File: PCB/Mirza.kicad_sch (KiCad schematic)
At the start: 105 parts, among them J1 In, J2 Out, J3 Power, Q1 BCM857BS, Q13 2SC3324, Q14 2SA1312, Q15 2SA1312, Q16 2SA1312, Q17 2SC3324, Q18 2SC3324, Q2 BCM847BS, Q21 2SA1312, Q22 2SC3324, Q23 2SC3324, Q24 2SA1312, Q25 D45H11, Q26 D44H11, Q3 2SA1312, Q4 2SC3324, Q5 2SC3324, Q6 2SC3324, Q7 2SA1312, Q8 2SA1312, U1 ADA4522-1

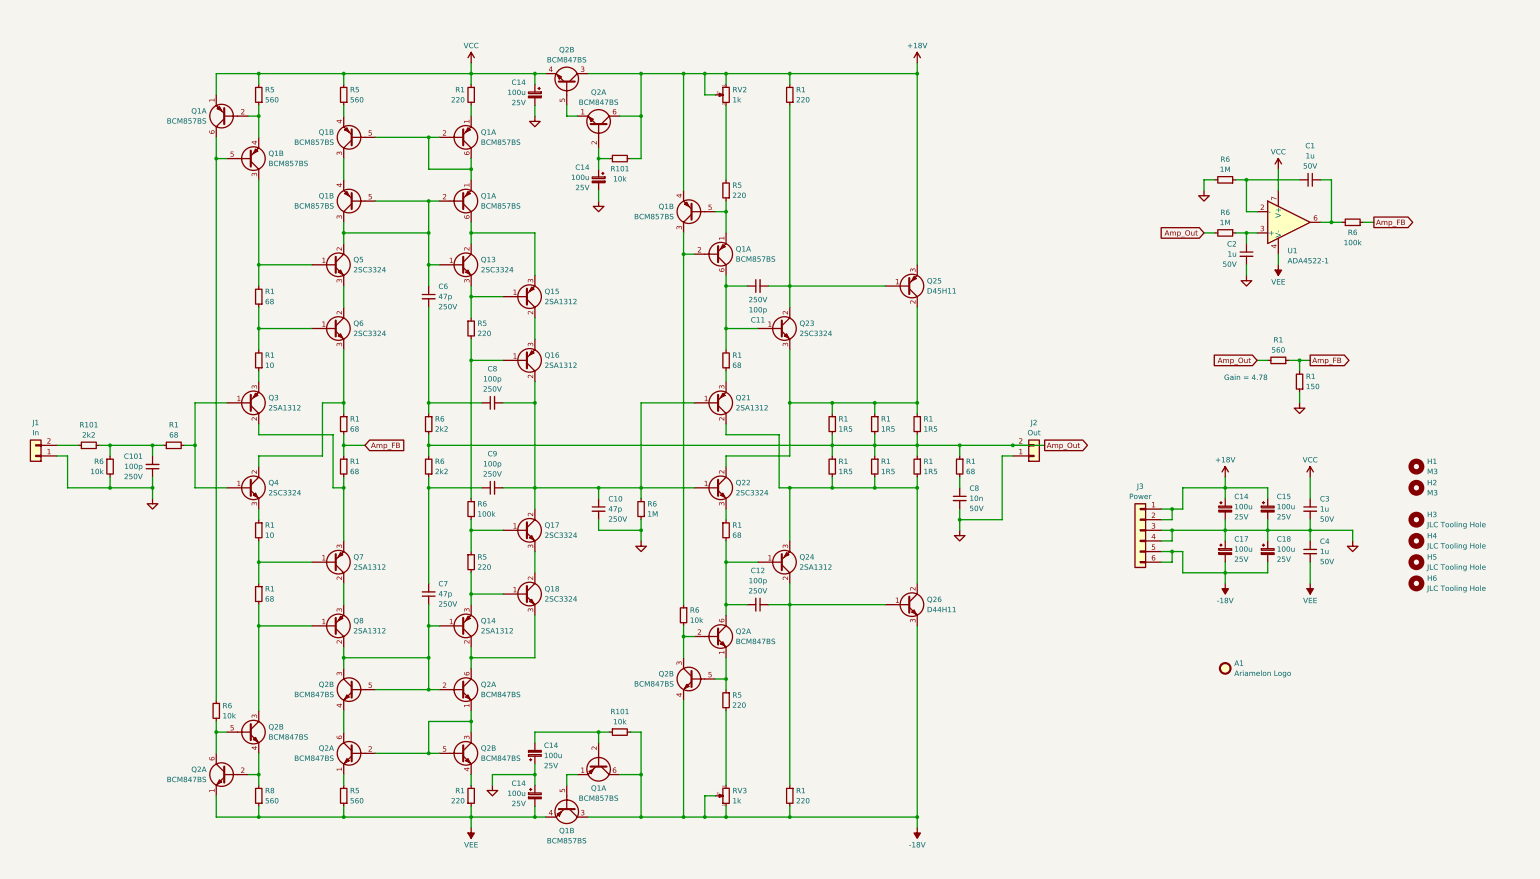
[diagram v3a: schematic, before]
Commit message: 20/09/2023 update
Shortened board by removing one pair of capacitors and increasing the size of the other and reducing the number of emitter resistors.
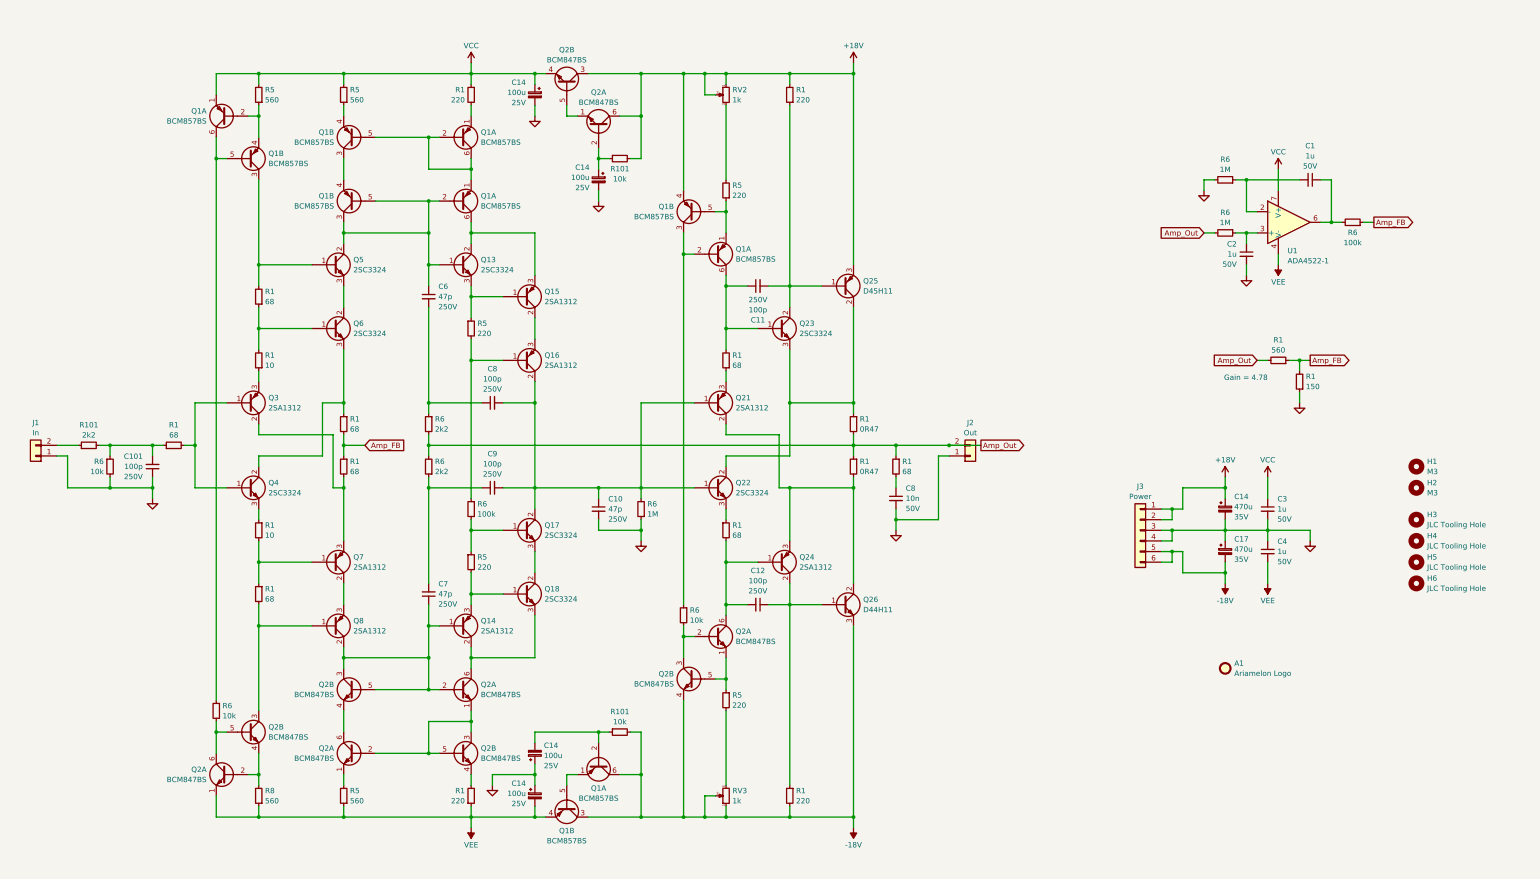
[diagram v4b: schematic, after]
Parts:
- removed C15, C18: 100u, Ariamelon-Device:CP_Radial_D6.3mm_P2.50mm, symbol Device:C_Polarized_Small
- removed R1 (x4): 1R5, Resistor_SMD:R_MiniMELF_MMA-0204, symbol Device:R_Small
- C14, C17: value 100u -> 470u; footprint Ariamelon-Device:CP_Radial_D6.3mm_P2.50mm -> Ariamelon-Device:CP_Radial_D8.0mm_P3.50mm_P5.00mm; LCSC C264049 -> C178717; Manufacturer No. EEUFR1E101 -> EEUFR1V471LB; Voltage 25V -> 35V
- R1: value 1R5 -> 0R47; LCSC C3008833 -> C2089943; Manufacturer No. MMA02040C1508FB300 -> MMA02040C4707FB300
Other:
- moved on the sheet: C3, C4, C8, J2, Q25, Q26, R1

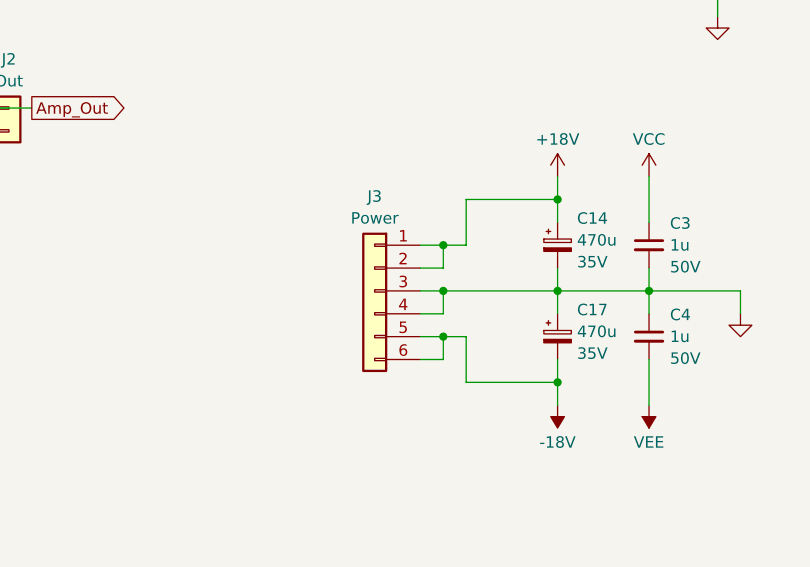
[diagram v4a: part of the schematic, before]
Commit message: 22/03/2023 update
Changed power connector to phoenix terminal block.
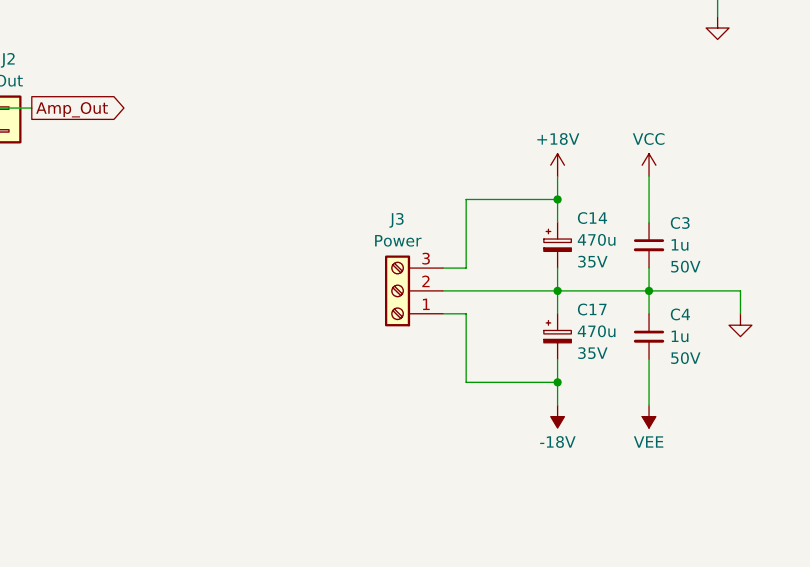
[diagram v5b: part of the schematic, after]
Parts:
- removed J3: Power, Ariamelon-Connector:JST_XH_B6B-XH-A_1x06_P2.50mm_Vertical_MiddleGND, symbol Connector_Generic:Conn_01x06
- added J3: Power, Ariamelon-Connector:TerminalBlock_Phoenix_MPT-0,5-3-2.54_1x03_P2.54mm_Horizontal_MiddleGND, symbol Connector:Screw_Terminal_01x03
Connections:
- net +18V: now also J3.3 (Pin_3)
- net -18V: now also J3.1 (Pin_1)
- net GND: now also J3.2 (Pin_2)
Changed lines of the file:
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@@
   (title_block
     (title "Mirza Current-Feedback Amplifier Module")
-    (date "2023-09-20")
+    (date "2023-09-22")
     (rev "V1.0")
     (company "Created by Ariamelon (https://github.com/Ariamelon/Mirza/)")
@@
   (junction (at 109.22 60.96) (diameter 0) (color 0 0 0 0)
   )
-  (junction (at 307.34 165.1) (diameter 0) (color 0 0 0 0)
-  )
   (junction (at 231.14 60.96) (diameter 0) (color 0 0 0 0)
   )
@@
   (junction (at 320.04 170.18) (diameter 0) (color 0 0 0 0)
   )
-  (junction (at 307.34 170.18) (diameter 0) (color 0 0 0 0)
-  )
   (junction (at 63.5 149.86) (diameter 0) (color 0 0 0 0)
   )
@@
   (junction (at 129.54 91.44) (diameter 0) (color 0 0 0 0)
   )
-  (junction (at 307.34 175.26) (diameter 0) (color 0 0 0 0)
-  )
   (junction (at 200.66 111.76) (diameter 0) (color 0 0 0 0)
   )
@@
     (stroke (width 0) (type default))
   )
-  (wire (pts (xy 307.34 175.26) (xy 309.88 175.26))
+  (wire (pts (xy 307.34 172.72) (xy 309.88 172.72))
     (stroke (width 0) (type default))
   )
@@
     (stroke (width 0) (type default))
   )
-  (wire (pts (xy 307.34 165.1) (xy 304.8 165.1))
-    (stroke (width 0) (type default))
-  )
-  (wire (pts (xy 307.34 172.72) (xy 307.34 170.18))
-    (stroke (width 0) (type default))
-  )
   (wire (pts (xy 144.78 228.6) (xy 154.94 228.6))
     (stroke (width 0) (type default))
@@
     (stroke (width 0) (type default))
   )
-  (wire (pts (xy 307.34 165.1) (xy 307.34 167.64))
-    (stroke (width 0) (type default))
-  )
   (wire (pts (xy 320.04 170.18) (xy 330.2 170.18))
     (stroke (width 0) (type default))
@@
     (stroke (width 0) (type default))
   )
-  (wire (pts (xy 304.8 172.72) (xy 307.34 172.72))
-    (stroke (width 0) (type default))
-  )
   (wire (pts (xy 88.9 60.96) (xy 109.22 60.96))
     (stroke (width 0) (type default))
@@
     (stroke (width 0) (type default))
   )
-  (wire (pts (xy 307.34 165.1) (xy 309.88 165.1))
+  (wire (pts (xy 307.34 167.64) (xy 309.88 167.64))
     (stroke (width 0) (type default))
   )
@@
     (stroke (width 0) (type default))
   )
-  (wire (pts (xy 309.88 180.34) (xy 309.88 175.26))
+  (wire (pts (xy 309.88 180.34) (xy 309.88 172.72))
     (stroke (width 0) (type default))
   )
@@
     (stroke (width 0) (type default))
   )
-  (wire (pts (xy 307.34 177.8) (xy 304.8 177.8))
-    (stroke (width 0) (type default))
-  )
   (wire (pts (xy 180.34 162.56) (xy 180.34 160.02))
     (stroke (width 0) (type default))
@@
     (stroke (width 0) (type default))
   )
-  (wire (pts (xy 309.88 165.1) (xy 309.88 160.02))
+  (wire (pts (xy 309.88 167.64) (xy 309.88 160.02))
     (stroke (width 0) (type default))
   )
@@
     (stroke (width 0) (type default))
   )
-  (wire (pts (xy 307.34 175.26) (xy 307.34 177.8))
-    (stroke (width 0) (type default))
-  )
   (wire (pts (xy 200.66 111.76) (xy 205.74 111.76))
     (stroke (width 0) (type default))
@@
     (stroke (width 0) (type default))
   )
-  (wire (pts (xy 304.8 175.26) (xy 307.34 175.26))
-    (stroke (width 0) (type default))
-  )
   (wire (pts (xy 63.5 160.02) (xy 63.5 157.48))
     (stroke (width 0) (type default))
@@
     (stroke (width 0) (type default))
   )
-  (wire (pts (xy 304.8 170.18) (xy 307.34 170.18))
-    (stroke (width 0) (type default))
-  )
   (wire (pts (xy 88.9 154.94) (xy 88.9 152.4))
     (stroke (width 0) (type default))
@@
     (stroke (width 0) (type default))
   )
-  (wire (pts (xy 307.34 167.64) (xy 304.8 167.64))
-    (stroke (width 0) (type default))
-  )
   (wire (pts (xy 139.7 68.58) (xy 139.7 71.12))
     (stroke (width 0) (type default))
@@
     )
   )
+  (symbol (lib_id "Connector:Screw_Terminal_01x03") (at 302.26 170.18 180) (unit 1)
+    (in_bom yes) (on_board yes) (dnp no) (fields_autoplaced)
+    (property "Reference" "J3" (at 302.26 162.2257 0)
+      (effects (font (size 1.27 1.27)))
+    )
+    (property "Value" "Power" (at 302.26 164.6499 0)
+      (effects (font (size 1.27 1.27)))
+    )
+    (property "Footprint" "Ariamelon-Connector:TerminalBlock_Phoenix_MPT-0,5-3-2.54_1x03_P2.54mm_Horizontal_MiddleGND" (at 302.26 170.18 0)
+      (effects (font (size 1.27 1.27)) hide)
+    )
+    (property "Datasheet" "~" (at 302.26 170.18 0)
+      (effects (font (size 1.27 1.27)) hide)
+    )
+    (pin "1")
+    (pin "2")
+    (pin "3")
+    (instances
+      (project "Mirza"
+        (path "/fe9fc43f-1188-4d03-8e81-9a6232eb6dc0"
+          (reference "J3") (unit 1)
+        )
+      )
+    )
+  )
   (symbol (lib_id "Device:R_Small") (at 88.9 185.42 0) (mirror y) (unit 1)
     (in_bom yes) (on_board yes) (dnp no)
@@
         )
       )
-    )
-  )
-  (symbol (lib_id "Connector_Generic:Conn_01x06") (at 299.72 170.18 0) (mirror y) (unit 1)
-    (in_bom yes) (on_board yes) (dnp no) (fields_autoplaced)
-    (property "Reference" "J3" (at 299.72 159.6857 0)
-      (effects (font (size 1.27 1.27)))
-    )
-    (property "Value" "Power" (at 299.72 162.1099 0)
-      (effects (font (size 1.27 1.27)))
-    )
-    (property "Footprint" "Ariamelon-Connector:JST_XH_B6B-XH-A_1x06_P2.50mm_Vertical_MiddleGND" (at 299.72 170.18 0)
-      (effects (font (size 1.27 1.27)) hide)
-    )
-    (property "Datasheet" "~" (at 299.72 170.18 0)
-      (effects (font (size 1.27 1.27)) hide)
-    )
-    (pin "1")
-    (pin "2")
-    (pin "3")
-    (pin "4")
-    (pin "5")
-    (pin "6")
-    (instances
-      (project "Mirza"
-        (path "/fe9fc43f-1188-4d03-8e81-9a6232eb6dc0"
-          (reference "J3") (unit 1)
-        )
-      )

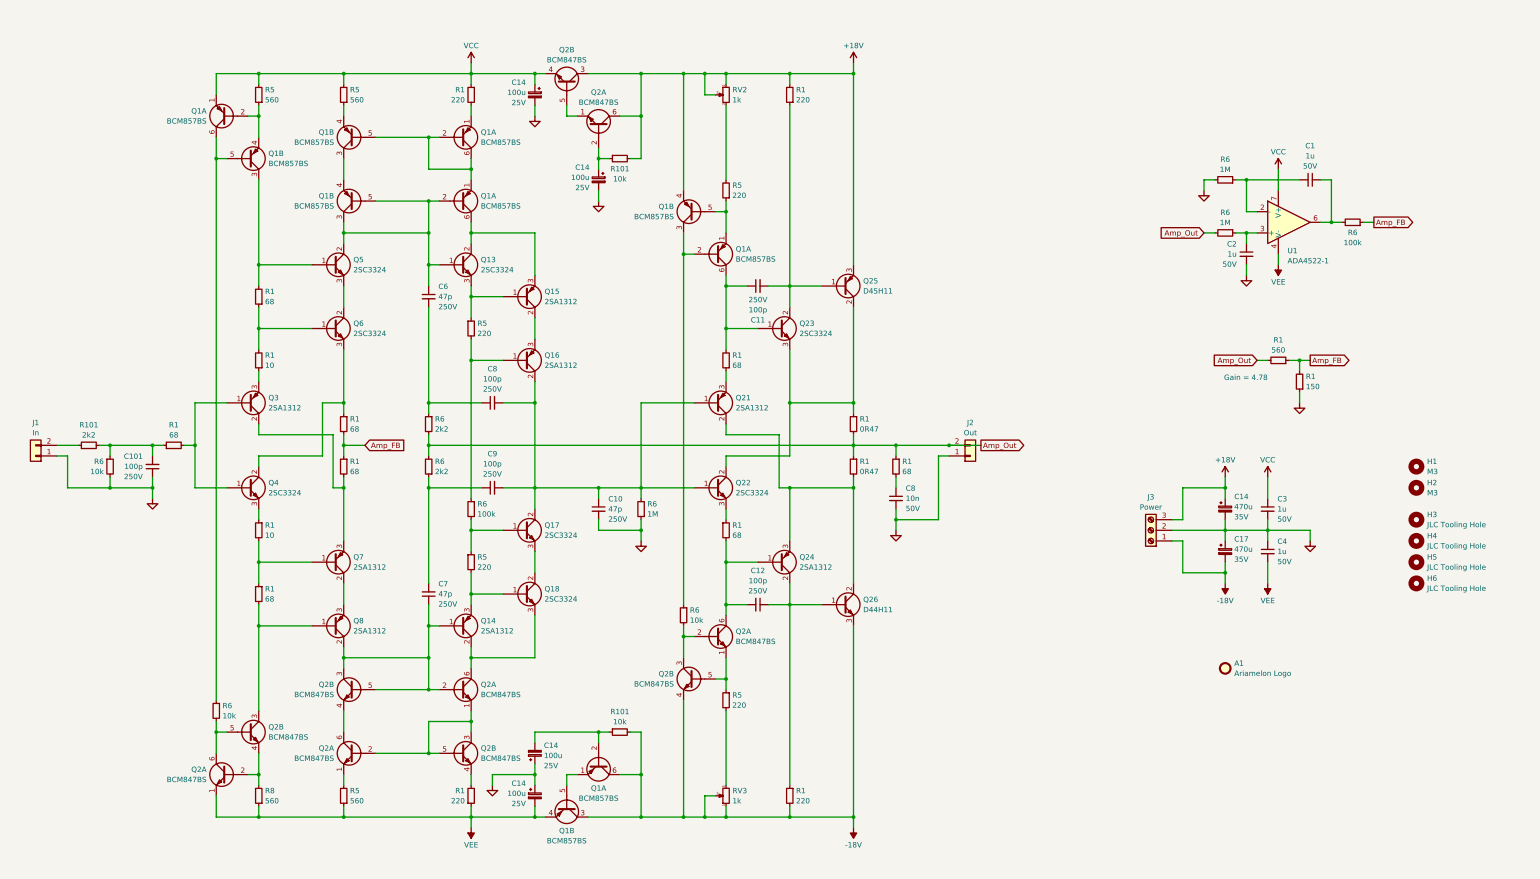
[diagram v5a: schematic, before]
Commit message: 23/09/2023 update
Changed all dual transistors to BCM847DS/BCM857DS for easier soldering.
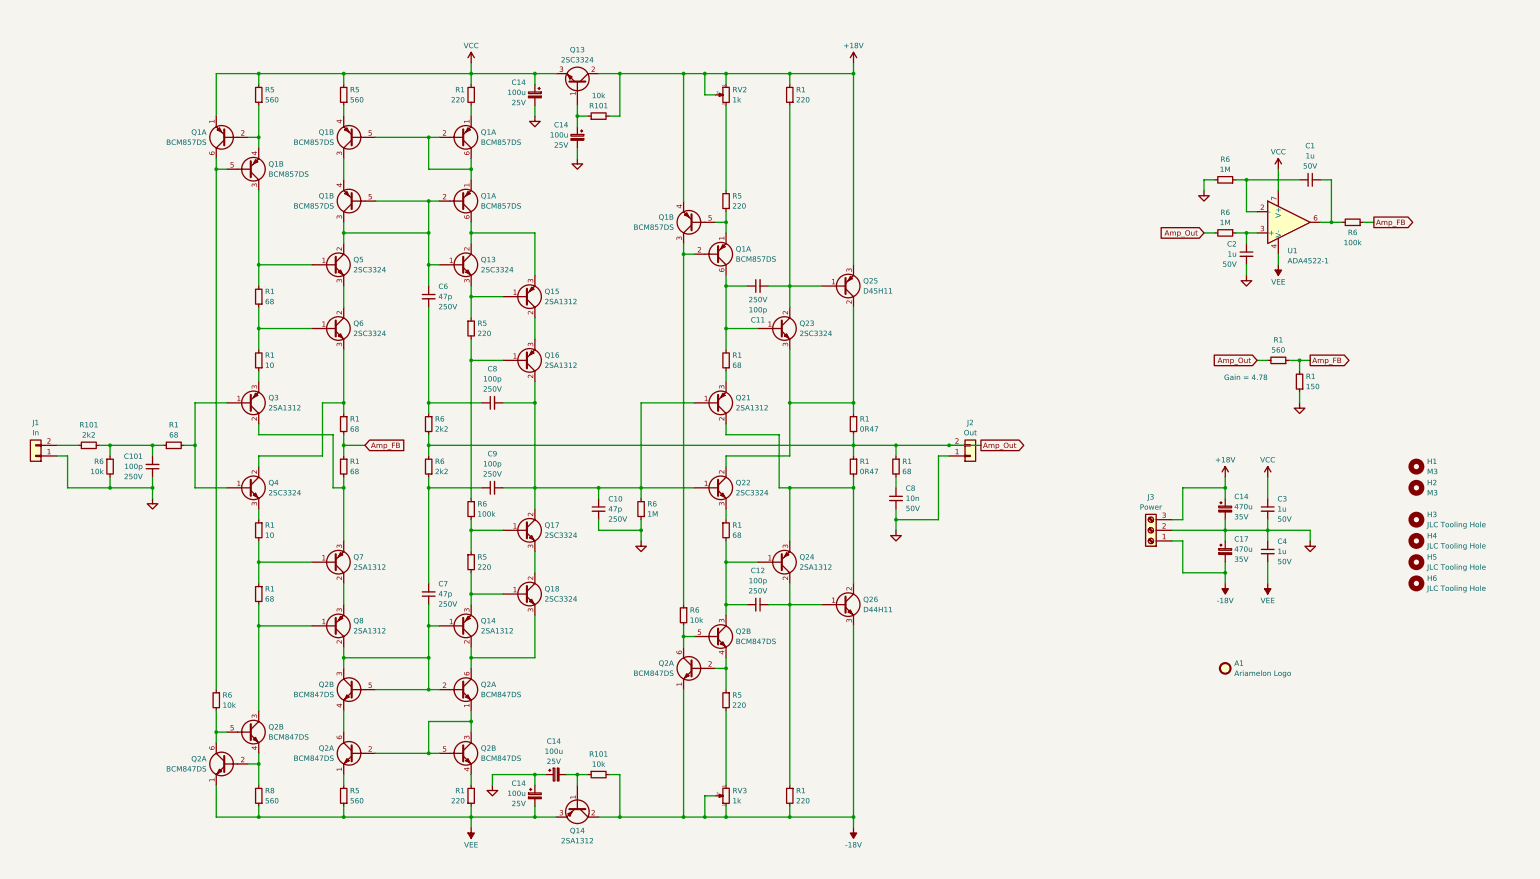
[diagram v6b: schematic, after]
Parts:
- removed Q1 (x5): BCM857BS, Ariamelon-Package:SOT-363_SC-70-6, symbol Transistor_BJT:BC857BS
- removed Q2 (x5): BCM847BS, Ariamelon-Package:SOT-363_SC-70-6, symbol Transistor_BJT:BC847BS
- added Q1 (x4): BCM857DS, Ariamelon-Package:SOT-23-6, symbol Device:Q_Dual_PNP_PNP_E1B1C2E2B2C1
- added Q13: 2SC3324, Ariamelon-Package:SOT-23-3, symbol Device:Q_NPN_BCE
- added Q14: 2SA1312, Ariamelon-Package:SOT-23-3, symbol Device:Q_PNP_BCE
- added Q2 (x4): BCM847DS, Ariamelon-Package:SOT-23-6, symbol Device:Q_Dual_NPN_NPN_E1B1C2E2B2C1
- J1, J2: Manufacturer No. (none) -> B2B-XH-A; now in the parts list
- J3: Manufacturer No. (none) -> 1725669
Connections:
- net +18V: now also Q1.4 (E2), Q13.2 (C)
- net -18V: now also Q14.2 (C), Q2.1 (E1)
- net VCC: now also Q1.1 (E1), Q13.3 (E)
- net VEE: now also Q14.3 (E), Q2.1 (E1)
- net at C11.1, Q23.1 (B), R1.2: now also Q1.6 (C1)
- net at R5.1: now also Q1.1 (E1), Q1.5 (B2)
- net at R6.1: now also Q1.2 (B1), Q1.3 (C2)
- net at C14.1, R101.1: now also Q13.1 (B)
- net at R5.1: now also Q1.2 (B1), Q1.4 (E2)
- net at R6.1: now also Q1.5 (B2), Q1.6 (C1)
- net at R1.2: now also Q2.4 (E2)
- net at R6.2: now also Q2.5 (B2), Q2.6 (C1) (x2)
- net at R5.1: now also Q2.2 (B1), Q2.4 (E2)
- net at Q14.2 (C), Q18.3 (E): now also Q2.6 (C1)
- net at C14.2, R101.1: now also Q14.1 (B)
- net at C6.1, Q13.1 (B), Q5.2 (C): now also Q1.2 (B1), Q1.3 (C2), Q1.5 (B2)
- net at Q5.1 (B), R1.2: now also Q1.3 (C2)
- net at C12.2, Q24.1 (B), R1.2: now also Q2.3 (C2)
- net at R5.2: now also Q2.1 (E1)
- net at R8.2: now also Q2.2 (B1), Q2.4 (E2)
- net at C7.1, Q14.1 (B), Q8.2 (C): now also Q2.2 (B1), Q2.3 (C2), Q2.5 (B2)
- net at Q8.1 (B), R1.2: now also Q2.3 (C2)
- net at R1.2: now also Q1.1 (E1)
- net at R5.1: now also Q1.4 (E2)
- net at Q13.2 (C), Q15.3 (E): now also Q1.6 (C1)
- new net: Q1.1 (E1), Q1.2 (B1), Q1.5 (B2), Q1.6 (C1)
- new net: Q1.3 (C2), Q1.4 (E2)
- new net: Q2.1 (E1), Q2.2 (B1), Q2.3 (C2), Q2.5 (B2)
- new net: Q2.4 (E2), Q2.6 (C1)
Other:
- moved on the sheet: C14, R101, R5, R6

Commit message: 24/09/2023 update
Increased thickness of power traces. Updated footprints for SOT-23-3 and SOT-23-6 footprints.
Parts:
- C14, C17: footprint Ariamelon-Device:CP_Radial_D8.0mm_P3.50mm_P5.00mm -> Capacitor_THT:CP_Radial_D8.0mm_P3.50mm
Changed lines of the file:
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@@
       (effects (font (size 1.27 1.27)) (justify left))
     )
-    (property "Footprint" "Ariamelon-Device:CP_Radial_D8.0mm_P3.50mm_P5.00mm" (at 320.04 175.26 0)
+    (property "Footprint" "Capacitor_THT:CP_Radial_D8.0mm_P3.50mm" (at 320.04 175.26 0)
       (effects (font (size 1.27 1.27)) hide)
     )
@@
       (effects (font (size 1.27 1.27)) (justify left))
     )
-    (property "Footprint" "Ariamelon-Device:CP_Radial_D8.0mm_P3.50mm_P5.00mm" (at 320.04 165.1 0)
-      (effects (font (size 1.27 1.27)) hide)
-    )
+    (property "Footprint" "Capacitor_THT:CP_Radial_D8.0mm_P3.50mm" (at 320.04 165.1 0)
+      (effects (font (size 1.27 1.27)) hide)
+    )
